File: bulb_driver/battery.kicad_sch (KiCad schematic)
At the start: 6 parts, among them Q1 DMG9926UDM, U3 AP9101CK6

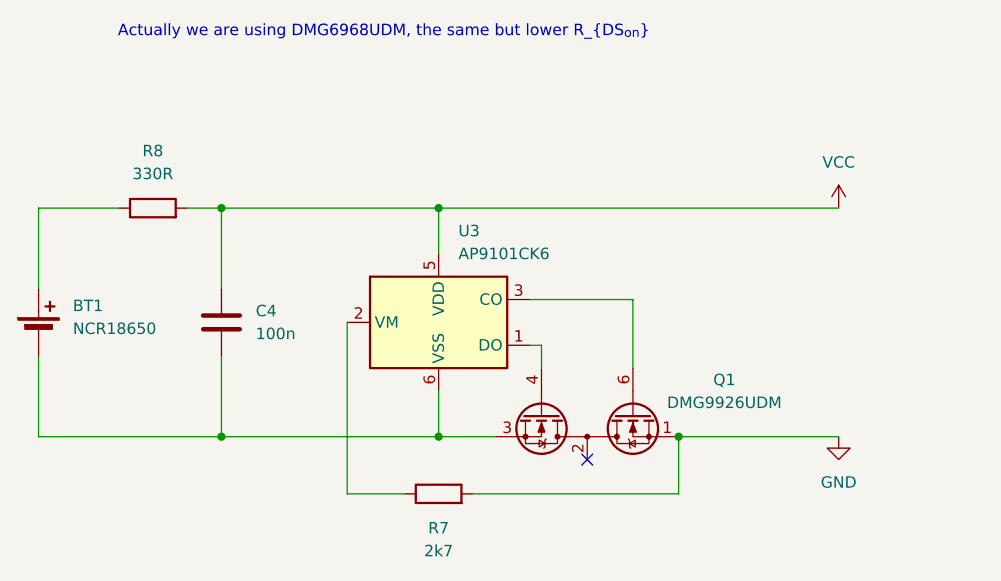
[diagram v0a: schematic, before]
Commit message: Add info text
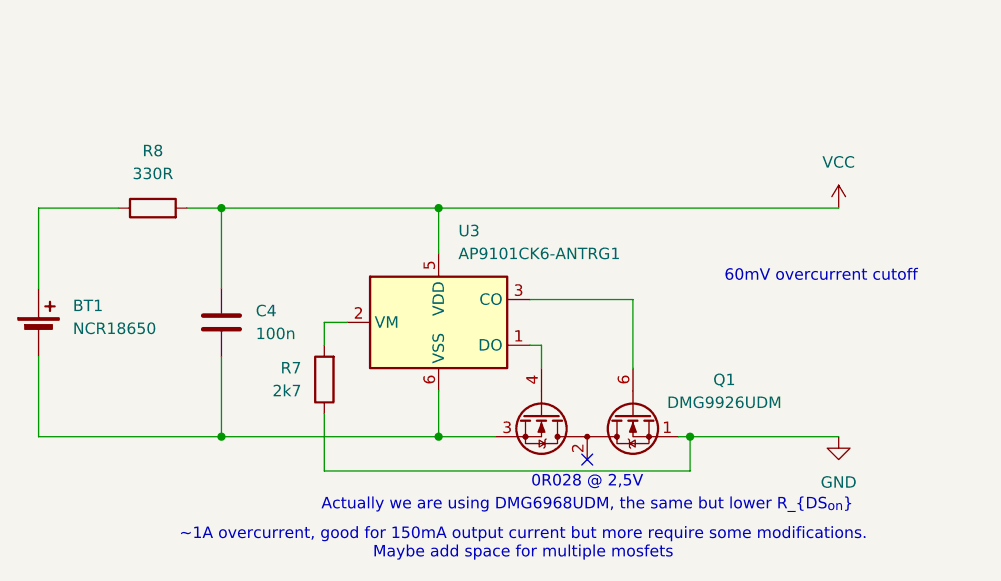
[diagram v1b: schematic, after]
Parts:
- U3: value AP9101CK6 -> AP9101CK6-ANTRG1
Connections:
- net GND: now also R7.1; no longer R7.2
- net at U3.2 (VM): now also R7.2; no longer R7.1
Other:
- note added: "0R028 @ 2,5V"
- note added: "60mV overcurrent cutoff"
- note added: "~1A overcurrent, good for 150mA output current but more require some modifications. Maybe add space for multiple mosfets"
- moved on the sheet: R7
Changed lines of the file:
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@@
-	)
-	(junction
-		(at 172.72 76.2)
-		(diameter 0)
-		(color 0 0 0 0)
 	)
 	(junction
@@
 		(color 0 0 0 0)
 	)
+	(junction
+		(at 173.99 76.2)
+		(diameter 0)
+		(color 0 0 0 0)
+	)
 	(no_connect
 		(at 162.56 78.74)
@@
 	(wire
 		(pts
-			(xy 172.72 82.55) (xy 172.72 76.2)
+			(xy 133.35 73.66) (xy 133.35 80.01)
 		)
 		(stroke
@@
 	(wire
 		(pts
+			(xy 133.35 80.01) (xy 173.99 80.01)
+		)
+		(stroke
+			(width 0)
+			(type default)
+		)
+	)
+	(wire
+		(pts
 			(xy 146.05 76.2) (xy 121.92 76.2)
 		)
@@
 	(wire
 		(pts
-			(xy 135.89 82.55) (xy 142.24 82.55)
-		)
-		(stroke
-			(width 0)
-			(type default)
-		)
-	)
-	(wire
-		(pts
 			(xy 118.11 50.8) (xy 121.92 50.8)
 		)
@@
 	(wire
 		(pts
-			(xy 135.89 63.5) (xy 135.89 82.55)
-		)
-		(stroke
-			(width 0)
-			(type default)
-		)
-	)
-	(wire
-		(pts
 			(xy 101.6 76.2) (xy 121.92 76.2)
 		)
@@
 	(wire
 		(pts
+			(xy 133.35 63.5) (xy 135.89 63.5)
+		)
+		(stroke
+			(width 0)
+			(type default)
+		)
+	)
+	(wire
+		(pts
 			(xy 101.6 59.69) (xy 101.6 50.8)
 		)
@@
 	(wire
 		(pts
-			(xy 172.72 76.2) (xy 190.5 76.2)
+			(xy 173.99 80.01) (xy 173.99 76.2)
+		)
+		(stroke
+			(width 0)
+			(type default)
+		)
+	)
+	(wire
+		(pts
+			(xy 172.72 76.2) (xy 173.99 76.2)
 		)
 		(stroke
@@
 	(wire
 		(pts
-			(xy 149.86 82.55) (xy 172.72 82.55)
-		)
-		(stroke
-			(width 0)
-			(type default)
-		)
-	)
-	(wire
-		(pts
 			(xy 146.05 50.8) (xy 121.92 50.8)
 		)
@@
 	(wire
 		(pts
+			(xy 173.99 76.2) (xy 190.5 76.2)
+		)
+		(stroke
+			(width 0)
+			(type default)
+		)
+	)
+	(wire
+		(pts
 			(xy 121.92 50.8) (xy 121.92 59.69)
 		)
@@
 		)
 	)
-	(text "Actually we are using DMG6968UDM, the same but lower R_{DS_{on}}"
-		(exclude_from_sim no)
-		(at 139.954 31.242 0)
+	(wire
+		(pts
+			(xy 133.35 66.04) (xy 133.35 63.5)
+		)
+		(stroke
+			(width 0)
+			(type default)
+		)
+	)
+	(text "~1A overcurrent, good for 150mA output current but more require some modifications.\nMaybe add space for multiple mosfets"
+		(exclude_from_sim no)
+		(at 155.448 88.138 0)
 		(effects
 			(font
@@
 		)
 	)
+	(text "0R028 @ 2,5V"
+		(exclude_from_sim no)
+		(at 162.56 81.28 0)
+		(effects
+			(font
+				(size 1.27 1.27)
+			)
+		)
+	)
+	(text "60mV overcurrent cutoff\n"
+		(exclude_from_sim no)
+		(at 177.8 58.42 0)
+		(effects
+			(font
+				(size 1.27 1.27)
+			)
+			(justify left)
+		)
+	)
+	(text "Actually we are using DMG6968UDM, the same but lower R_{DS_{on}}"
+		(exclude_from_sim no)
+		(at 162.56 83.82 0)
+		(effects
+			(font
+				(size 1.27 1.27)
+			)
+		)
+	)
 	(symbol
 		(lib_id "Device:R")
-		(at 146.05 82.55 90)
+		(at 133.35 69.85 180)
 		(unit 1)
 		(exclude_from_sim no)
@@
 		(fields_autoplaced yes)
 		(property "Reference" "R7"
-			(at 146.05 86.36 90)
-			(effects
-				(font
-					(size 1.27 1.27)
-				)
+			(at 130.81 68.5799 0)
+			(effects
+				(font
+					(size 1.27 1.27)
+				)
+				(justify left)
 			)
 		)
 		(property "Value" "2k7"
-			(at 146.05 88.9 90)
-			(effects
-				(font
-					(size 1.27 1.27)
-				)
+			(at 130.81 71.1199 0)
+			(effects
+				(font
+					(size 1.27 1.27)
+				)
+				(justify left)
 			)
 		)
 		(property "Footprint" ""
-			(at 146.05 84.328 90)
+			(at 135.128 69.85 90)
 			(effects
 				(font
@@
 		)
 		(property "Datasheet" "~"
-			(at 146.05 82.55 0)
+			(at 133.35 69.85 0)
 			(effects
 				(font
@@
 		)
 		(property "Description" "Resistor"
-			(at 146.05 82.55 0)
+			(at 133.35 69.85 0)
 			(effects
 				(font
@@
 			)
 		)
-		(property "Value" "AP9101CK6"
+		(property "Value" "AP9101CK6-ANTRG1"
 			(at 148.2441 55.88 0)
 			(effects
